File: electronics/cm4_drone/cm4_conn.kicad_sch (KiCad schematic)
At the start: 5 parts, among them U5 Compute_Module_4_Connectors

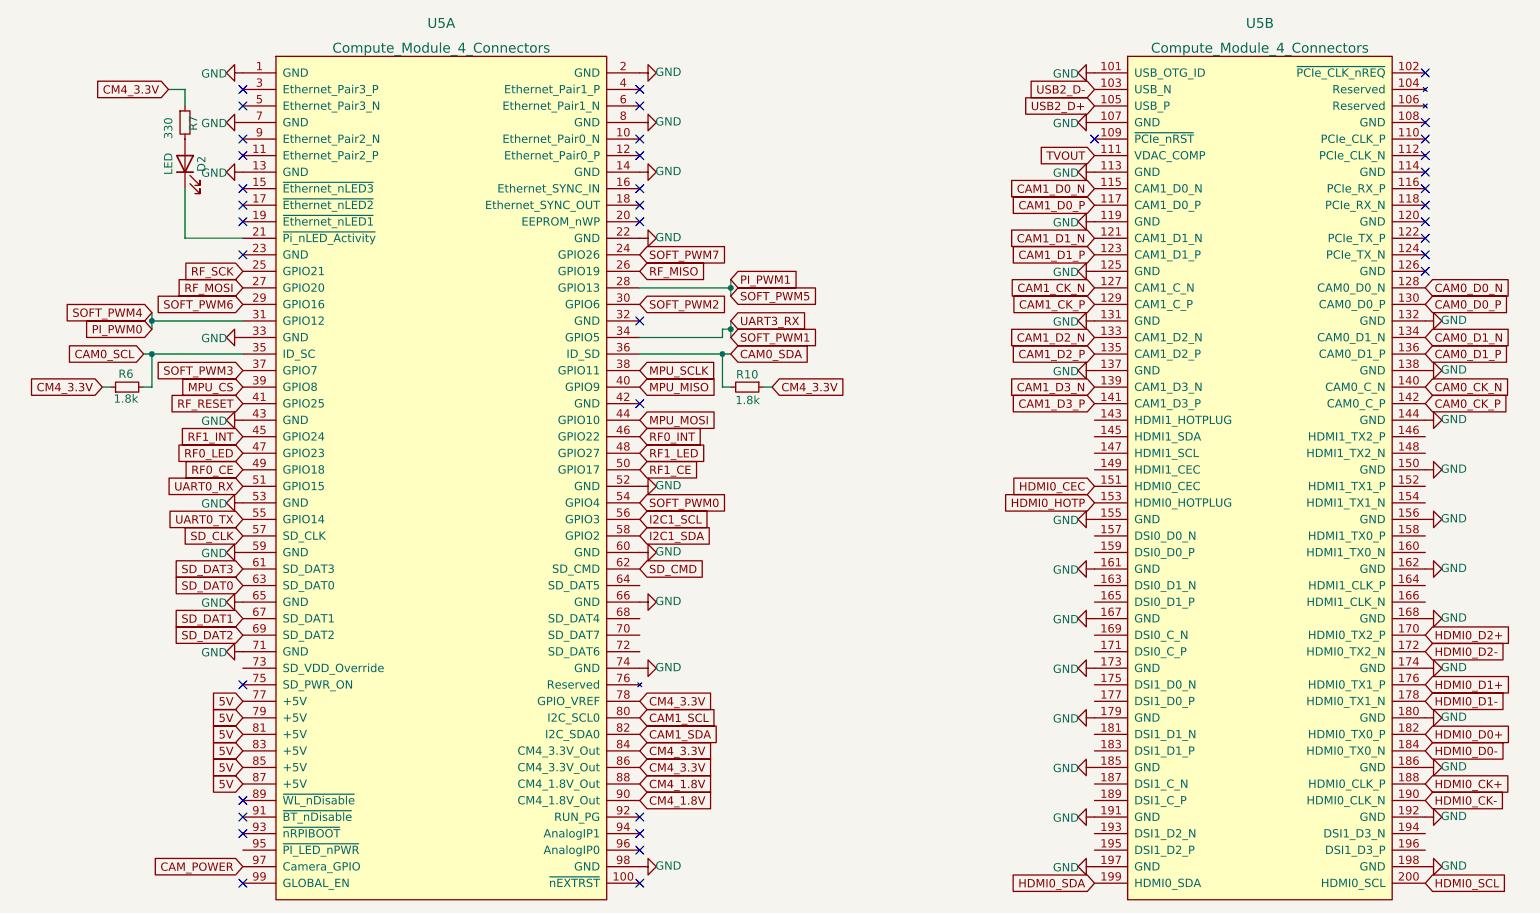
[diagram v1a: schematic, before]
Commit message: electronics: fix labels shapes
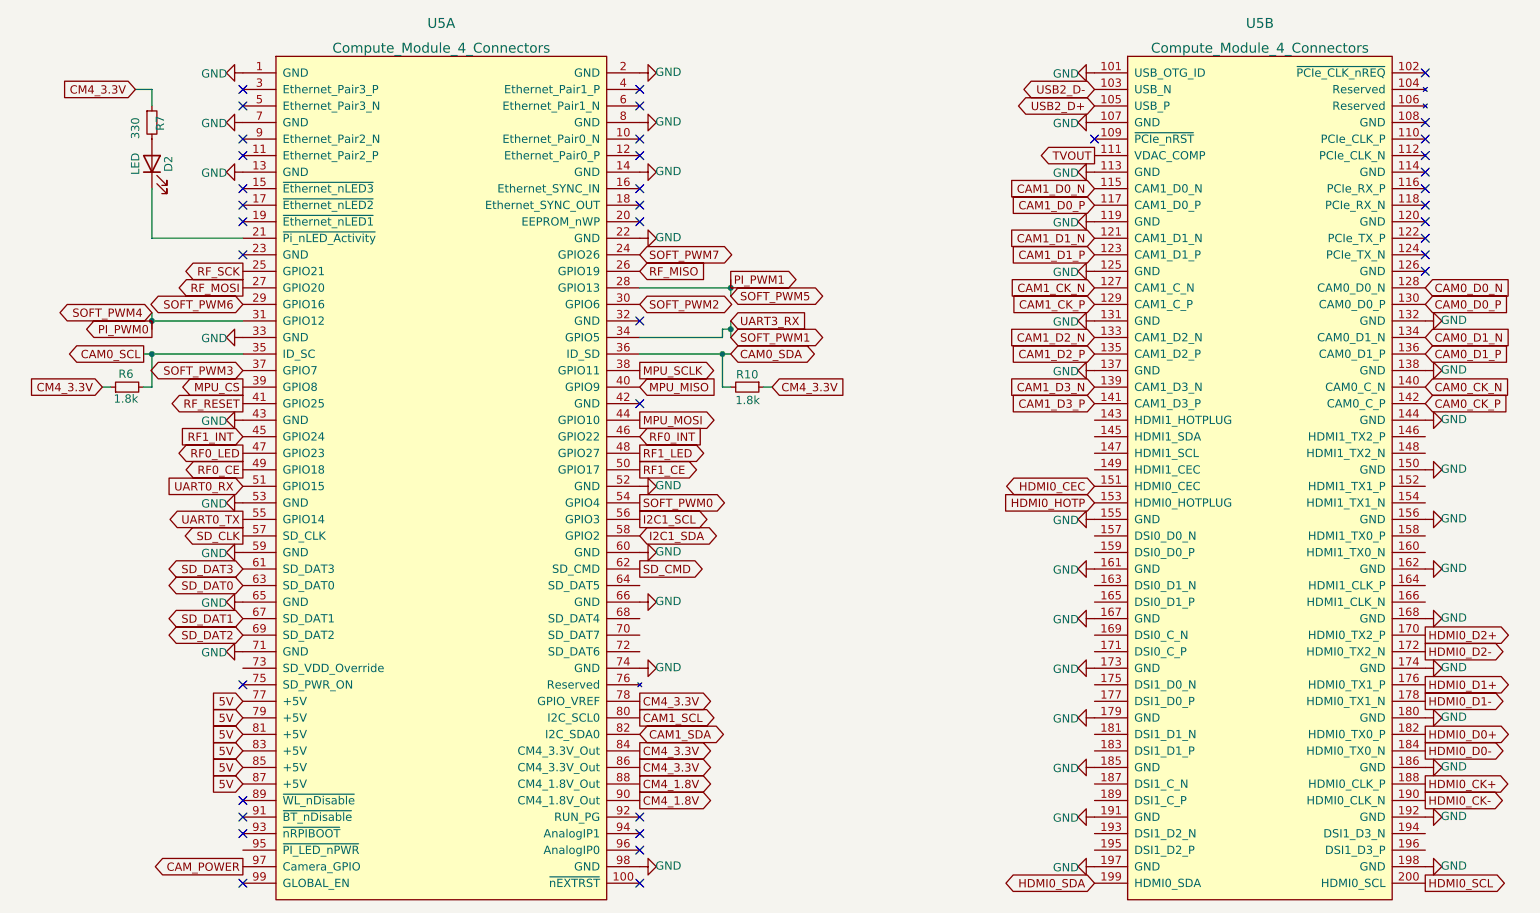
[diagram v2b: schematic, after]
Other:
- moved on the sheet: D2, R7
